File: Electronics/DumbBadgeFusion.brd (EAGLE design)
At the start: 163.5 x 113 mm, 151 parts, among them IC1 74245MTC, IC2 74245MTC, IC3 74245MTC, SW1 SPST_TACT-KMR2, T1 MMUN2133LT1G, U1 ATSAMD21J18A-AUT, U2 TPS61090RSAR, U3 MCP73871, U4 FAN5333BSX, U5 TPD3E001SOT5, U6 MAX3232, X4 NX3215SA-32.768K-STD-MUA-8

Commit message: might be done?
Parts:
- moved C13 2.54 mm to (124.8, 92.6)
- moved U6 2.54 mm to (119.5, 96.3)
- moved C22 2.54 mm to (124.7, 99.5)
- moved C23 2.54 mm to (124.8, 96.3)
- moved C24 2.54 mm to (126.4, 99.5)
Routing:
- net GND: track 174.2 -> 300.7 mm, vias 28 -> 56
- net USB_N: track 134.5 -> 216.3 mm, vias 3 -> 6
- net USB_P: track 132.0 -> 212.9 mm, vias 1 -> 4
- net UART_TX: track 93.1 -> 159.8 mm, vias 3 -> 4
- net UART_RX: track 98.1 -> 162.5 mm, vias 5 -> 6
- net KEYROW3: track 229.4 -> 292.3 mm, vias 10 -> 12
- net 5.0V: track 270.7 -> 333.4 mm, vias 2 -> 4
- net KEYROW8: track 202.4 -> 260.2 mm, vias 11 -> 14
- net KEYROW9: track 214.5 -> 265.2 mm, vias 8 -> 11
- net KEYROW1: track 119.2 -> 167.2 mm, vias 7 -> 8
- net KEYROW7: track 303.0 -> 349.5 mm, vias 14 -> 17
- net +24V: track 0.41 -> 40.1 mm, vias 0 -> 2
- net LEDK: track 5.69 -> 44.6 mm, vias 0 -> 2
- net KEYROW0: track 83.7 -> 121.2 mm, vias 0 -> 3
- net SWDIO: track 42.9 -> 77.0 mm, vias 2 -> 3
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
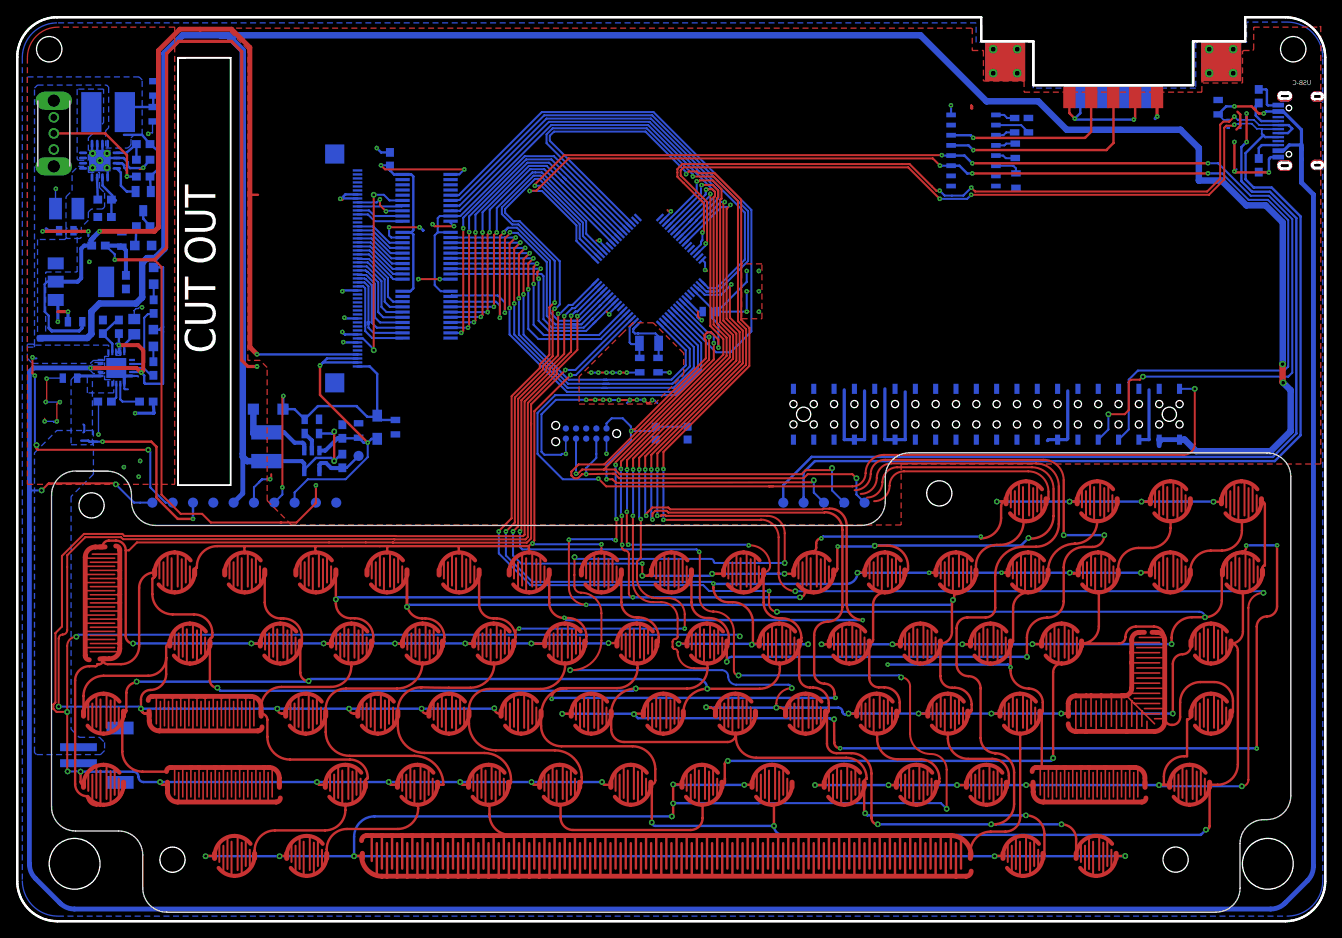
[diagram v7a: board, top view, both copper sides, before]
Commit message: moved +24V gen, cleanup
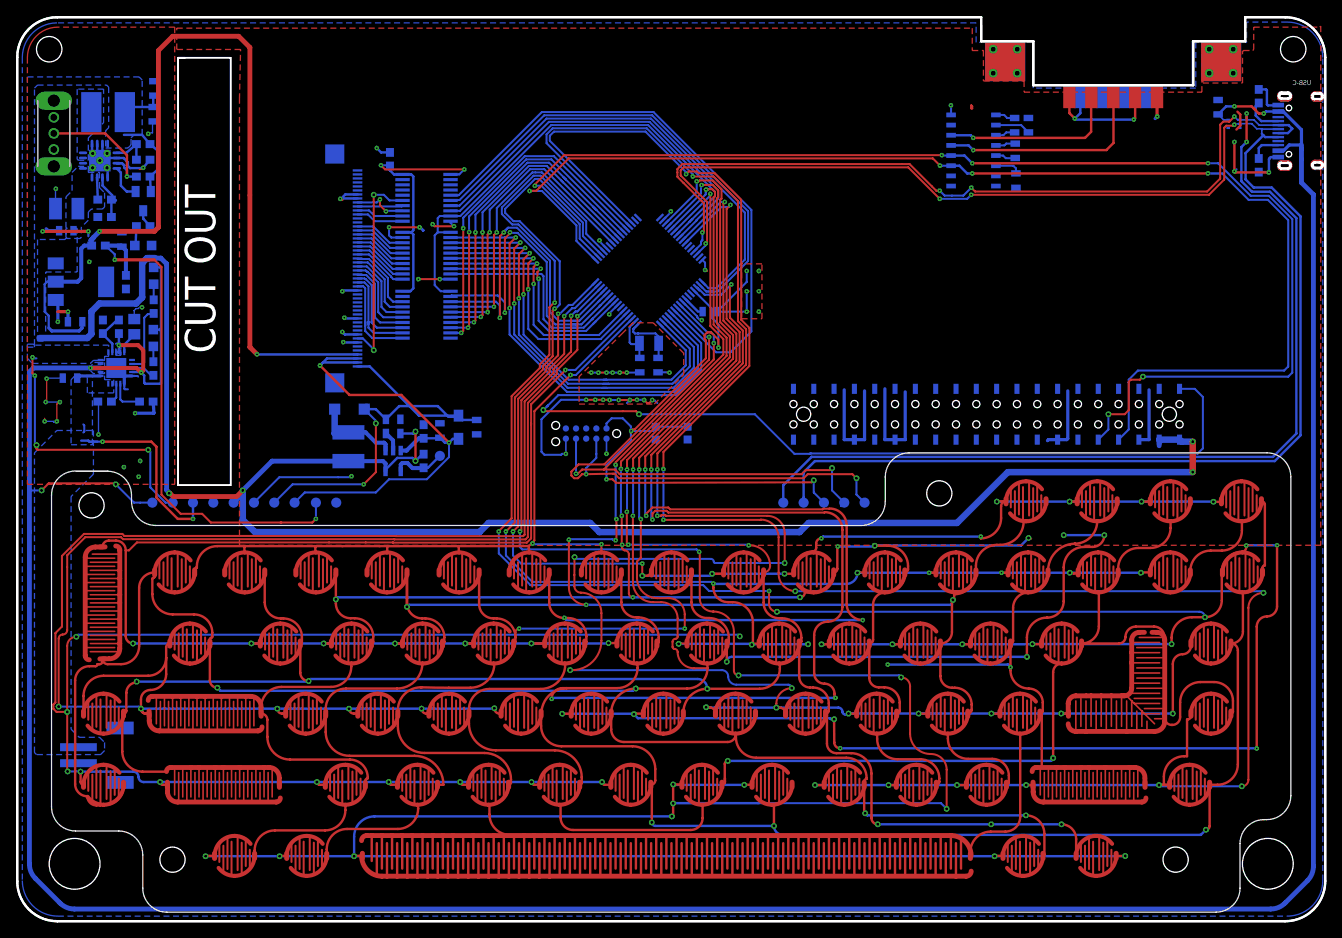
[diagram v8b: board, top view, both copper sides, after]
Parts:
- moved C11 10.2 mm to (47.0, 62.7)
- moved C8 10.2 mm to (47.0, 61.0)
- moved C9 10.2 mm to (52.8, 61.3)
- moved D2 10.2 mm to (41.5, 64.0)
- moved TP17 10.2 mm to (52.8, 58.2)
- moved U4 10.2 mm to (47.0, 57.5)
- moved L2 10.2 mm to (41.4, 59.3)
- moved C10 10.2 mm to (57.4, 61.8)
- moved D1 10.2 mm to (55.2, 61.7)
- moved R1 10.2 mm to (50.8, 57.5)
- moved R12 10.2 mm to (50.8, 61.2)
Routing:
- net 5.0V: track 333.4 -> 239.7 mm, vias 4 -> 6
- net KEYCOLUM1: track 367.9 -> 286.0 mm
- net 1.8V: track 148.5 -> 67.5 mm, vias 3 -> 2
- net GND: track 300.7 -> 257.2 mm
- net KEYCOLUM0: track 405.9 -> 370.2 mm
- net KEYCOLUM2: track 303.7 -> 270.3 mm
- net KEYCOLUM3: track 288.2 -> 262.4 mm
- net LEDK: track 44.6 -> 62.0 mm
- net +24V: track 40.1 -> 54.6 mm
- net PB31: track 131.8 -> 125.4 mm
- net 3V3: track 149.9 -> 153.6 mm
- net VBUS: track 402.5 -> 401.2 mm
